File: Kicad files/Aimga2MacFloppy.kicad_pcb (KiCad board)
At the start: 2 copper layers, 44 x 54 mm, 12 parts, among them J1 DB23F, J2 Conn_02x10_Odd_Even_MountingP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, J3 DB23M, U1 74LS139, U2 74LS393

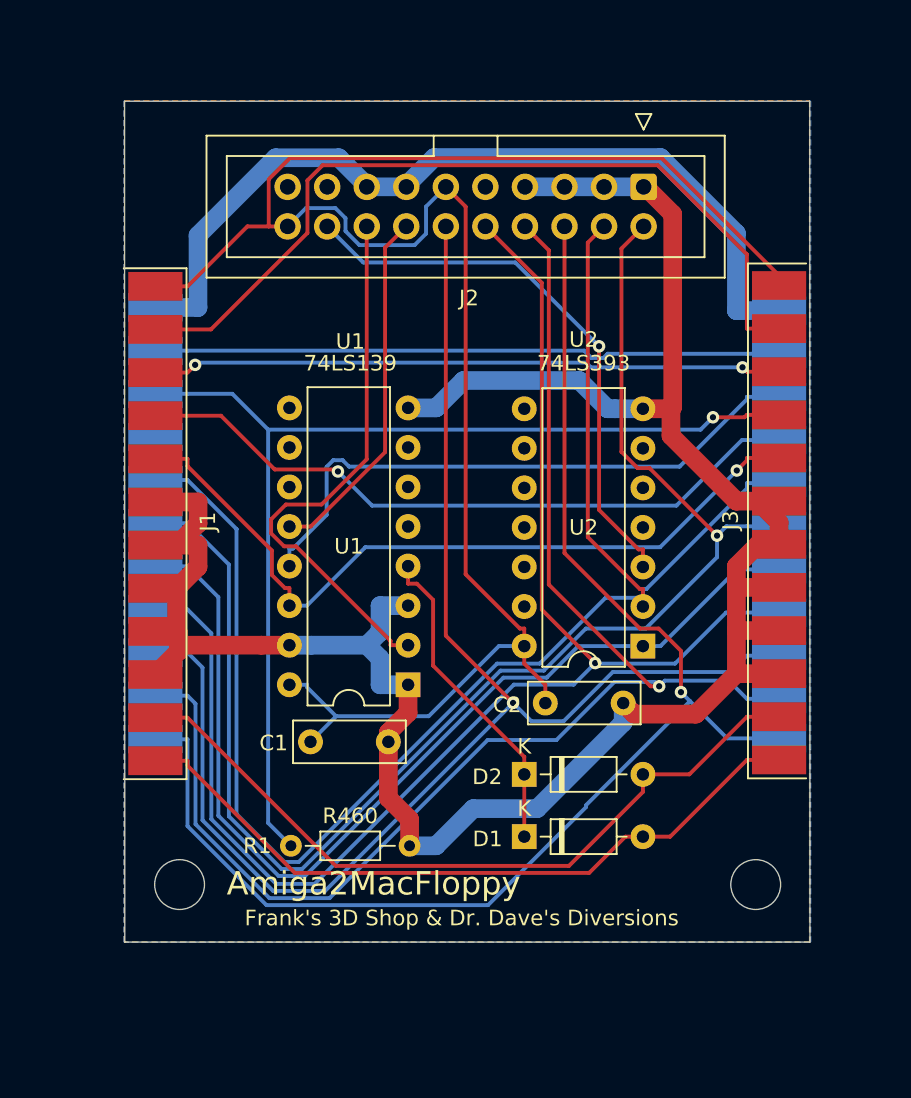
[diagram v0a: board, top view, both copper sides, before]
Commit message: Change size
Changed the size for an Amiga 2000 to clear the RCA mono out jack.
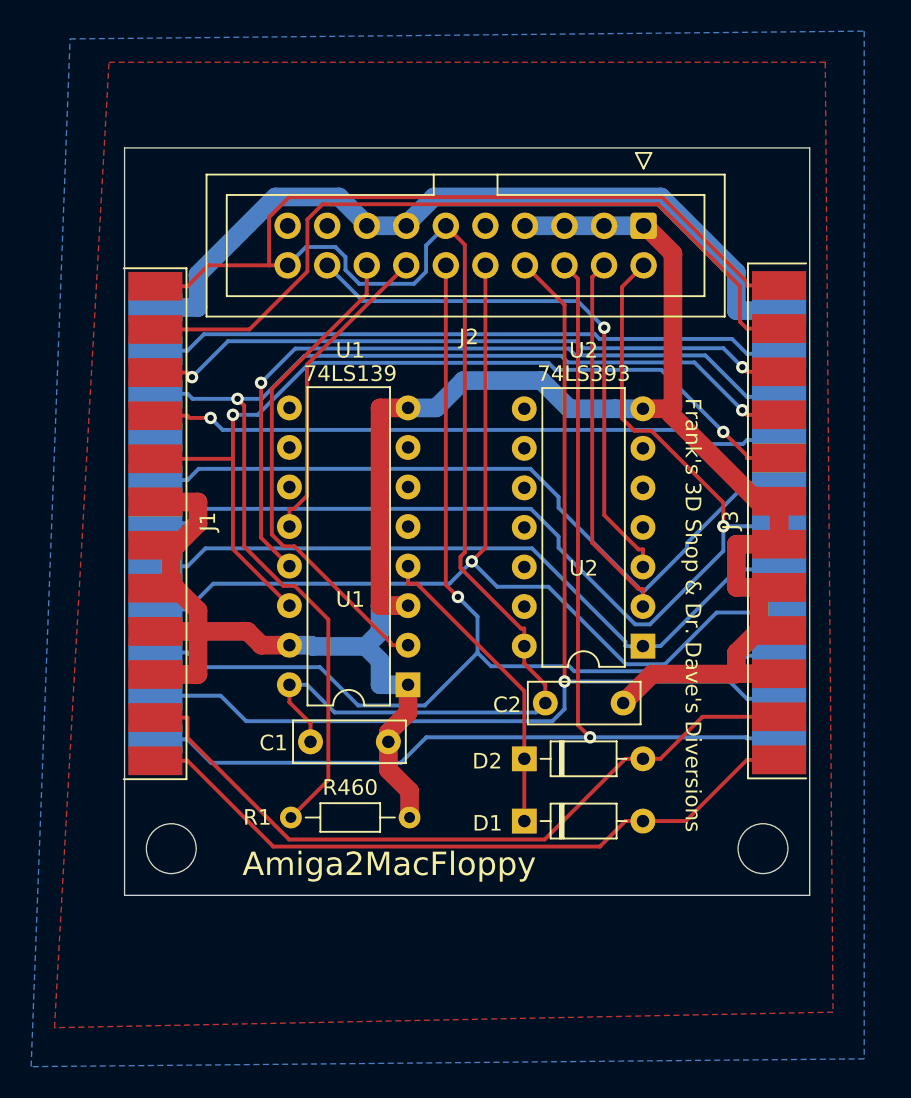
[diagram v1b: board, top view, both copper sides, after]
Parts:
- moved J2 2.50 mm to (149.8, 85.7)
- moved Hole1 2.37 mm to (119.5, 125.7)
- moved Hole2 2.35 mm to (157.5, 125.7)
- moved R460 1.82 mm to (127.2, 123.7)
- moved D1 1.00 mm to (142.1, 123.9)
- moved D2 1.00 mm to (142.1, 119.9)
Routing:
- net _DKWE: track 92.6 -> 64.8 mm
- net DIR: track 98.5 -> 71.8 mm
- net PH0: track 92.1 -> 68.1 mm
- net SEL: track 91.8 -> 69.5 mm
- net _DKWD: track 64.7 -> 45.3 mm
- net PH3: track 89.9 -> 71.1 mm
- net PH2: track 88.8 -> 72.4 mm
- net _SEL1: track 38.8 -> 48.0 mm, vias 0 -> 1
- net _MTRXD: track 49.8 -> 57.8 mm, vias 1 -> 2
- net GND: track 154.2 -> 147.5 mm
- net +12V: track 55.4 -> 50.3 mm
- net _SEL2: track 68.7 -> 73.6 mm, vias 1 -> 2
- net RD: track 35.5 -> 31.6 mm
- net _CHNG: track 53.5 -> 50.0 mm
- net _SEL3: track 44.2 -> 40.9 mm
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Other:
- board size 44 x 54 mm -> 44 x 48 mm
- board text added: "Frank's 3D Shop & Dr. Dave's Diversions https://github.com/Franks3dShop/Amiga2MacFloppy"
- board text removed: "Frank's 3D Shop https://github.com/Franks3dShop/Amiga2MacFloppy"

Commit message: Smaller Case
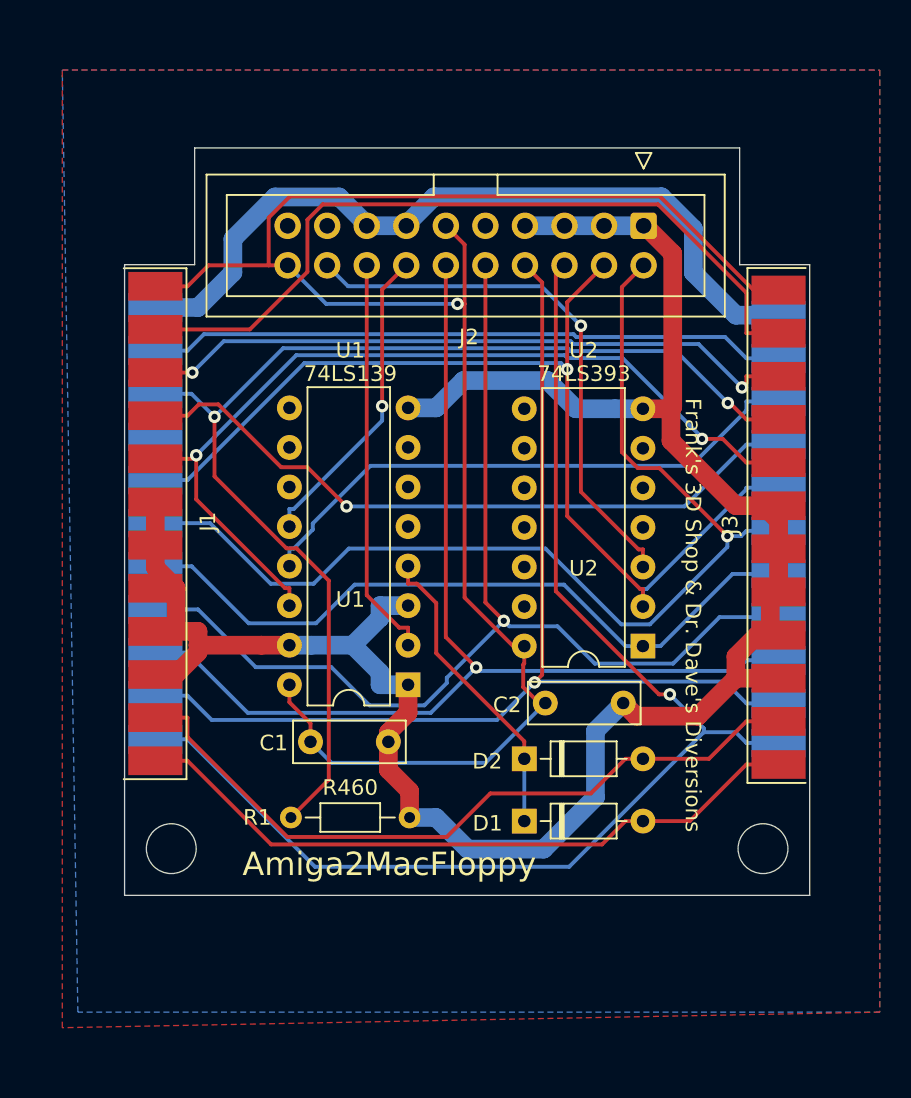
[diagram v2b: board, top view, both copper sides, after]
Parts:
- moved J3 0.29 mm to (158.5, 105.2)
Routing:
- net _SEL1: track 48.0 -> 37.0 mm, vias 1 -> 0
- net PH2: track 72.4 -> 81.8 mm
- net _DKWE: track 64.8 -> 70.7 mm
- net RD: track 31.6 -> 25.8 mm
- net GND: track 147.5 -> 142.9 mm
- net DIR: track 71.8 -> 67.3 mm, vias 0 -> 1
- net _SEL3: track 40.9 -> 44.7 mm
- net PWM: track 117.8 -> 116.0 mm, vias 0 -> 1
- net PH3: track 71.1 -> 69.7 mm
- net PH0: track 68.1 -> 69.1 mm
- net _SEL2: track 73.6 -> 74.5 mm
- net WR: track 36.0 -> 35.2 mm
- net _DKWD: track 45.3 -> 46.1 mm
- net _DRES: track 41.9 -> 42.6 mm
- net _ENABLE: vias 0 -> 1
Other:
- outline, holes or cut-outs redrawn
